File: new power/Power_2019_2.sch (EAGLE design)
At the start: 59 parts, among them IC1 ATMEGA328P_PDIP, IC2 LT1161, IC4 LT1161, Q5 16MHz, Q8 16MHz, U1 MCP2515, X1 MABC96R

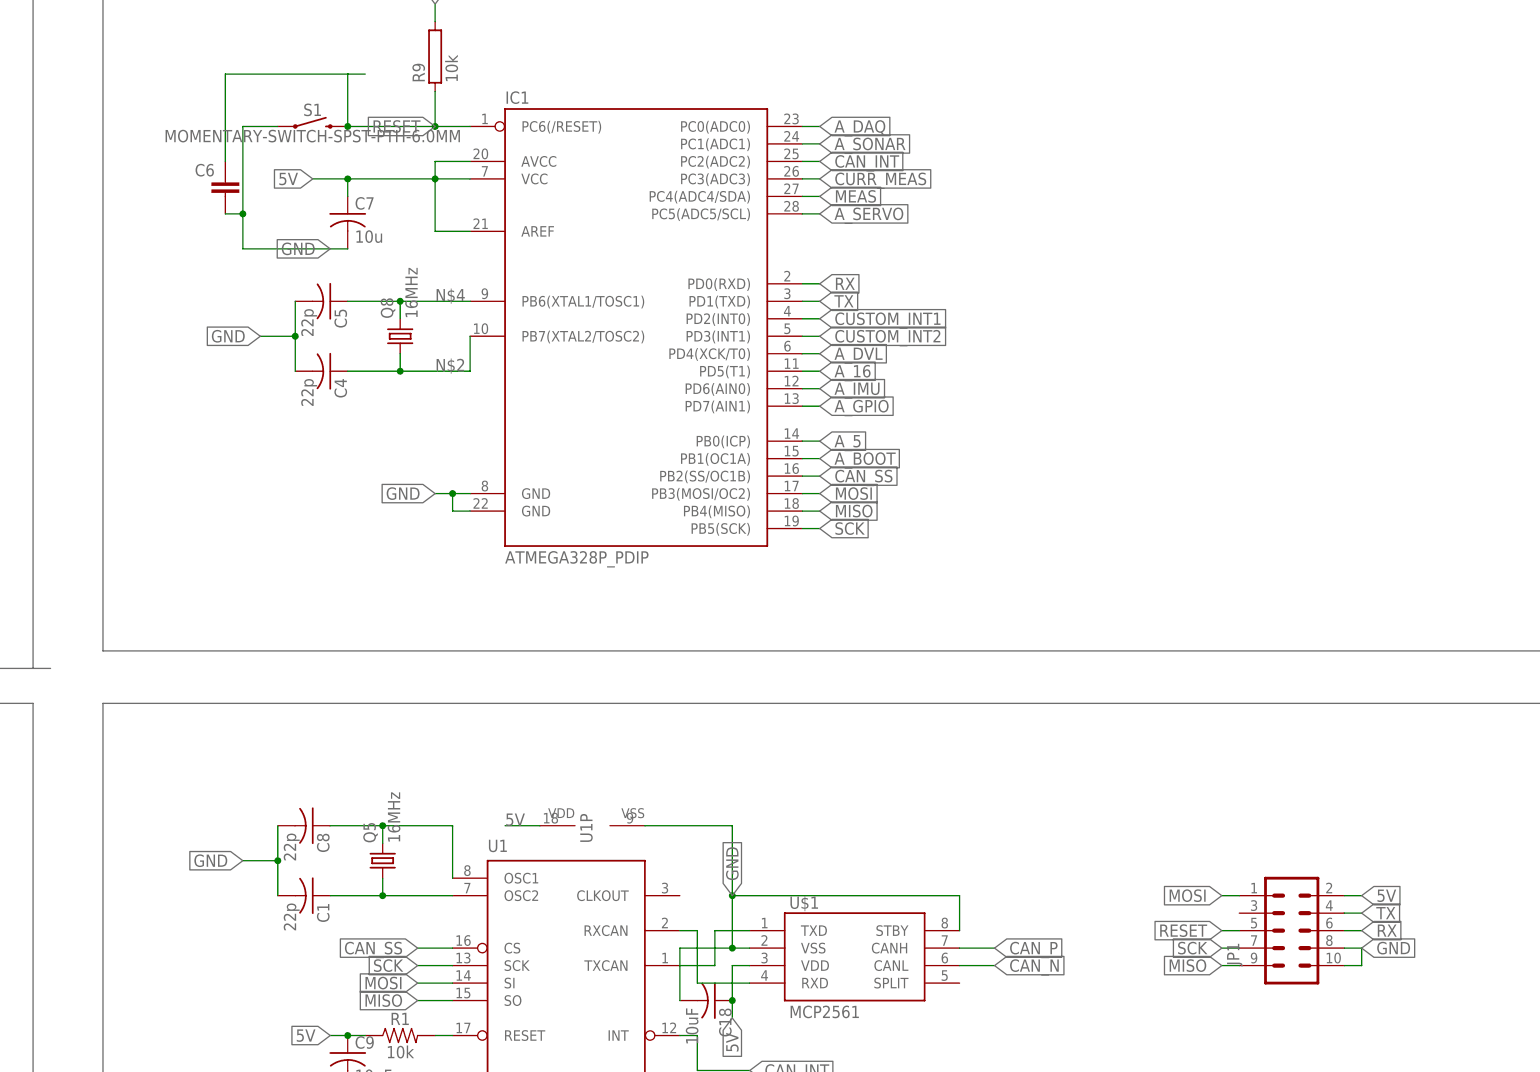
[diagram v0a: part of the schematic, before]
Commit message: power board without labelling
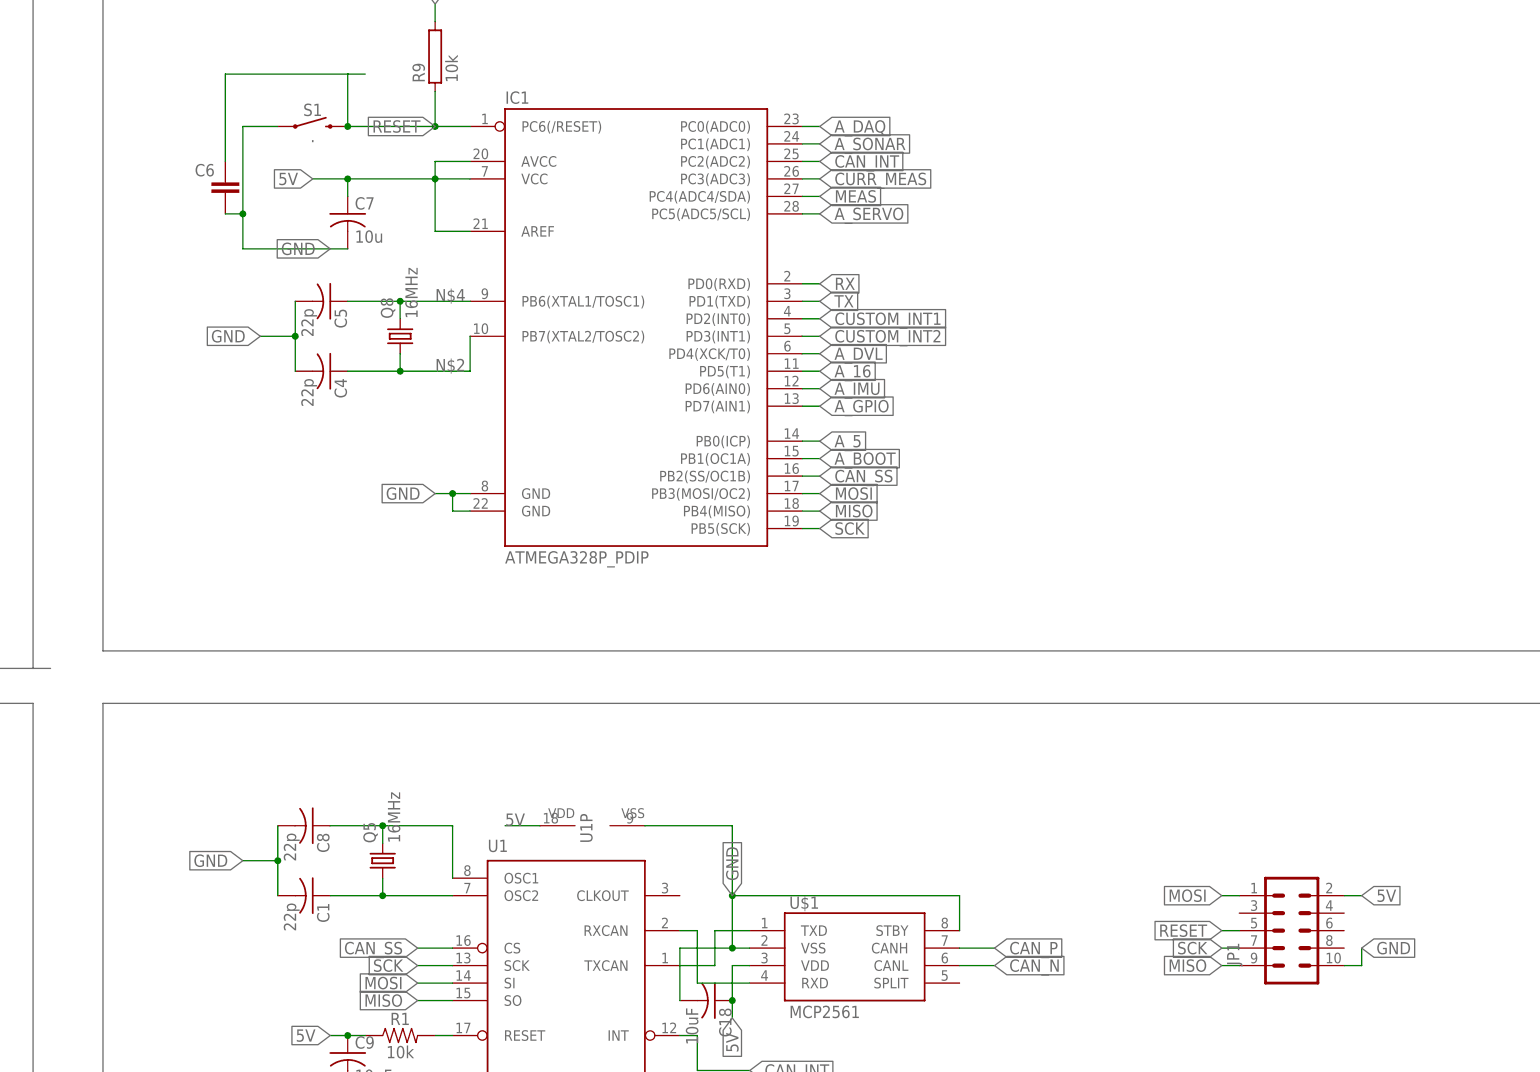
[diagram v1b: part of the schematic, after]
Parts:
- S1: value MOMENTARY-SWITCH-SPST-PTH-6.0MM -> .
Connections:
- net GND: no longer JP1.8
- net RX: no longer JP1.6
- net TX: no longer JP1.4
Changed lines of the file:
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@@
 <part name="RI3" library="rcl" library_urn="urn:adsk.eagle:library:334" deviceset="R-EU_" device="M0805" package3d_urn="urn:adsk.eagle:package:23556/2" value="100"/>
 <part name="C18" library="adafruit" library_urn="urn:adsk.eagle:library:420" deviceset="C-US" device="025-050X050" package3d_urn="urn:adsk.eagle:package:6240320/1" value="10uF"/>
-<part name="S1" library="SparkFun-Switches" library_urn="urn:adsk.eagle:library:535" deviceset="MOMENTARY-SWITCH-SPST" device="-PTH-6.0MM" package3d_urn="urn:adsk.eagle:package:40163/1"/>
+<part name="S1" library="SparkFun-Switches" library_urn="urn:adsk.eagle:library:535" deviceset="MOMENTARY-SWITCH-SPST" device="-PTH-6.0MM" package3d_urn="urn:adsk.eagle:package:40163/1" value=" ."/>
 <part name="X1" library="con-vg" library_urn="urn:adsk.eagle:library:194" deviceset="MABC96R" device="">
 <attribute name="MF" value=""/>
@@
 <wire x1="-223.52" y1="-167.64" x2="-223.52" y2="-170.18" width="0.1524" layer="91"/>
 <wire x1="-223.52" y1="-170.18" x2="-226.06" y2="-170.18" width="0.1524" layer="91"/>
-<pinref part="JP1" gate="G$1" pin="8"/>
-<wire x1="-226.06" y1="-167.64" x2="-223.52" y2="-167.64" width="0.1524" layer="91"/>
 <label x="-223.52" y="-167.64" size="1.778" layer="95" xref="yes"/>
 </segment>
@@
 </segment>
 <segment>
-<pinref part="JP1" gate="G$1" pin="6"/>
-<wire x1="-226.06" y1="-165.1" x2="-223.52" y2="-165.1" width="0.1524" layer="91"/>
-<label x="-223.52" y="-165.1" size="1.778" layer="95" xref="yes"/>
-</segment>
-<segment>
 <pinref part="X1" gate="-A3" pin="S"/>
 <wire x1="-599.44" y1="-144.78" x2="-614.68" y2="-144.78" width="0.1524" layer="91"/>
@@
 </segment>
 <segment>
-<pinref part="JP1" gate="G$1" pin="4"/>
-<wire x1="-226.06" y1="-162.56" x2="-223.52" y2="-162.56" width="0.1524" layer="91"/>
-<label x="-223.52" y="-162.56" size="1.778" layer="95" xref="yes"/>
-</segment>
-<segment>

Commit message: FINAL BY LK WITHOUT LABELLING
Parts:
- removed JP3: (no value), jumper:JP1E
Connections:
- net GND: no longer JP3.1
- net PTN_INH: no longer JP3.2
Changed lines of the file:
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@@
 <part name="C10" library="rcl" deviceset="CPOL-EU" device="E2.5-5" value="330uF"/>
 <part name="U$5" library="ptn78060wah" deviceset="PTN78060WAH" device=""/>
-<part name="JP3" library="jumper" library_urn="urn:adsk.eagle:library:252" deviceset="JP1E" device="" package3d_urn="urn:adsk.eagle:package:15455/1"/>
 <part name="RI1" library="rcl" library_urn="urn:adsk.eagle:library:334" deviceset="R-EU_" device="M0805" package3d_urn="urn:adsk.eagle:package:23556/2" value="100"/>
 <part name="IC4" library="LT1161" deviceset="ROBOSUB_LINEAR-TECHNOLOGY_LT1161_QUAD-HIGH-SIDE-MOSFET-DRIVER_LT1161-SO20" device="SW" value="LT1161"/>
@@
 <attribute name="VALUE" x="-469.9" y="-160.02" size="1.778" layer="96"/>
 </instance>
-<instance part="JP3" gate="A" x="-500.38" y="-154.94" smashed="yes" rot="R90">
-<attribute name="NAME" x="-500.38" y="-156.21" size="1.778" layer="95" rot="R180"/>
-<attribute name="VALUE" x="-500.38" y="-149.225" size="1.778" layer="96" rot="R180"/>
-</instance>
 <instance part="RI1" gate="G$1" x="-579.12" y="-83.82" smashed="yes" rot="R180">
 <attribute name="NAME" x="-575.31" y="-85.3186" size="1.778" layer="95" rot="R180"/>
@@
 <wire x1="-449.58" y1="-181.61" x2="-449.58" y2="-187.96" width="0.1524" layer="91"/>
 <label x="-449.58" y="-187.96" size="1.778" layer="95" rot="R180" xref="yes"/>
-</segment>
-<segment>
-<pinref part="JP3" gate="A" pin="1"/>
-<wire x1="-497.84" y1="-154.94" x2="-495.3" y2="-154.94" width="0.1524" layer="91"/>
-<label x="-495.3" y="-154.94" size="1.778" layer="95" xref="yes"/>
 </segment>
 <segment>
@@
 <label x="-480.06" y="-200.66" size="1.778" layer="95" rot="R270" xref="yes"/>
 </segment>
-<segment>
-<pinref part="JP3" gate="A" pin="2"/>
-<wire x1="-497.84" y1="-152.4" x2="-495.3" y2="-152.4" width="0.1524" layer="91"/>
-<label x="-495.3" y="-152.4" size="1.778" layer="95" xref="yes"/>
-</segment>
-</net>
+</net>
